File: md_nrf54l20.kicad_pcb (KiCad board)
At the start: 2 copper layers, 51.6 x 42 mm, 6 parts, among them J1 USB_C_Receptacle_USB2.0_16P, U1 nRF54L20

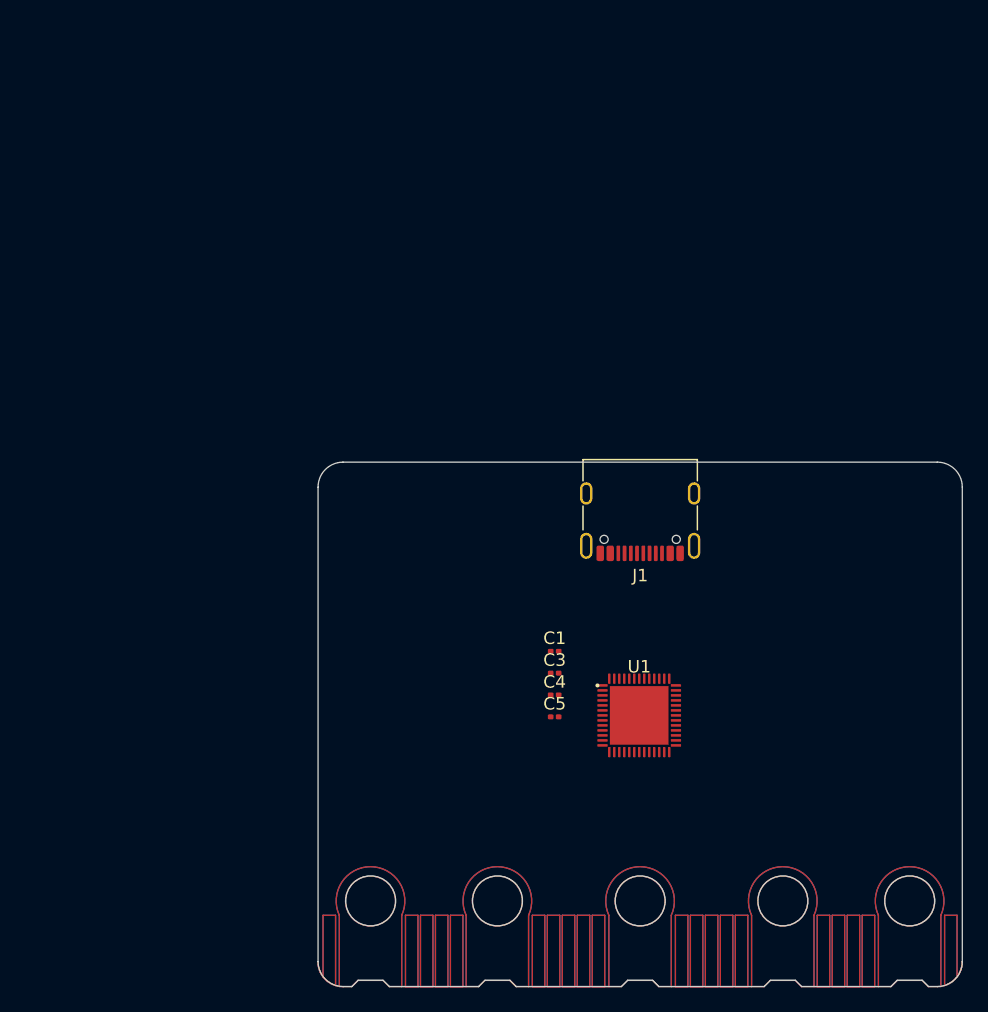
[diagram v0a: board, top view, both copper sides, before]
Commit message: Promote v2 and add Uno R3 shield headers
- circuit_v2.json -> circuit.json (single source); generated to the project
  root md_nrf54l20.kicad_sch; md_nrf54l20-v2.kicad_sch removed.
- Board: copied the ~/uno R3 form-factor PCB over md_nrf54l20.kicad_pcb
  (J1-J4 header sockets + 4 mounting holes); added Arduino_MountingHole.pretty
  and registered it in fp-lib-table.
- Wired the Uno headers to the nRF with function-correct pins: A0-A5 on ADC
  channels (AIN0-4 + AIN7), AREF on EXTREF, UART on D0/D1, SPI on D10-D13,
  PWM-capable pins on D3/D5/D6/D9/D10/D11; I2C SDA/SCL shared with A4/A5.
- Renumbered existing connectors so the Uno headers can be J1-J4: USB-C -> J5,
  SWD -> J6. Moved speaker PWM P1.06 -> P2.01 to free P1.06 for analog A4.

Co-Authored-By: Claude Opus 4.8 <noreply@anthropic.com>
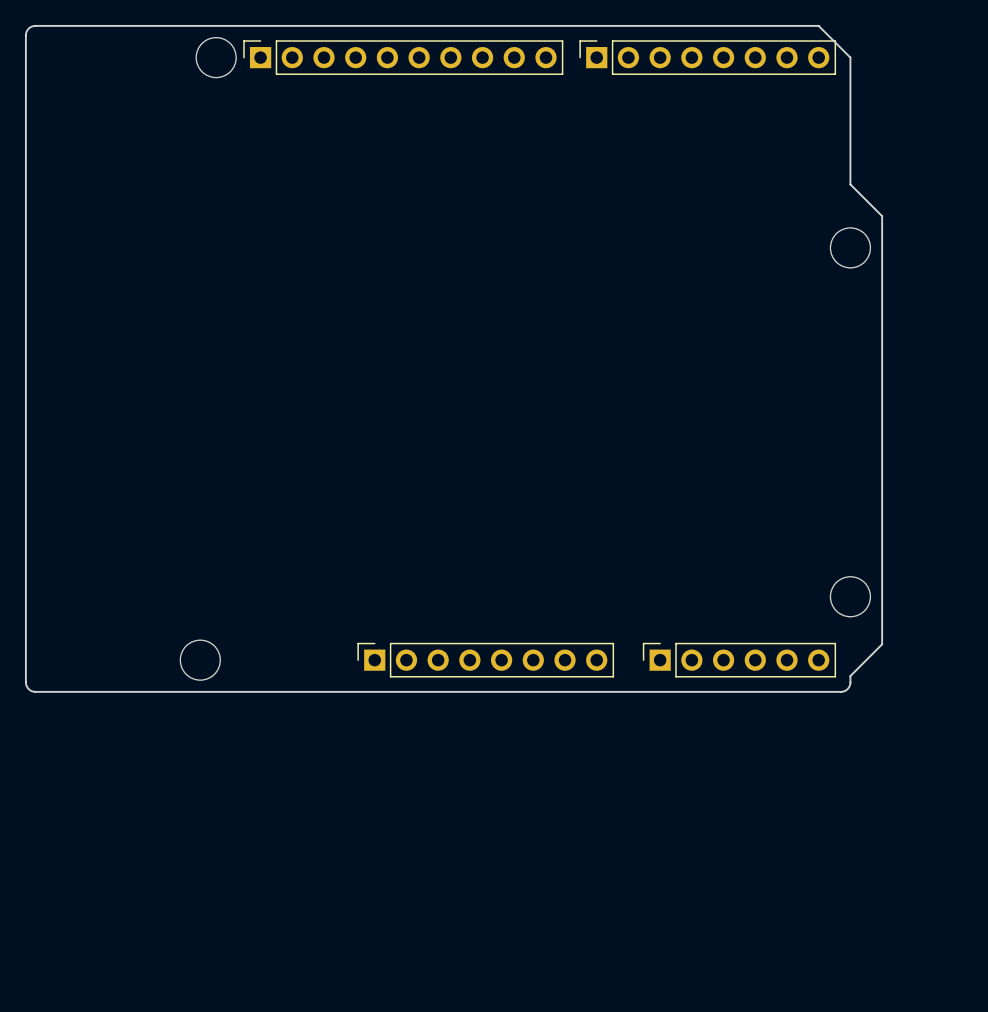
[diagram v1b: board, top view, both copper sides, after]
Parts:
- removed C1: 10uF, Capacitor_SMD:C_0201_0603Metric
- removed C3, C4, C5: 100nF, Capacitor_SMD:C_0201_0603Metric
- removed U1: nRF54L20, md_nrf54l20:QFN-52-1EP_6x6mm_P0.4mm_EP4.7x4.7mm
- added J2: Digital/PWM, Connector_PinSocket_2.54mm:PinSocket_1x10_P2.54mm_Vertical, F.Cu at (118.8, 49.2)
- added J3: Analog, Connector_PinSocket_2.54mm:PinSocket_1x06_P2.54mm_Vertical, F.Cu at (150.8, 97.5)
- added J4: Digital/PWM, Connector_PinSocket_2.54mm:PinSocket_1x08_P2.54mm_Vertical, F.Cu at (145.7, 49.2)
- added MH1: MountingHole_3.2mm, Arduino_MountingHole:MountingHole_3.2mm, F.Cu at (115.2, 49.2)
- added MH2: MountingHole_3.2mm, Arduino_MountingHole:MountingHole_3.2mm, F.Cu at (114.0, 97.5)
- added MH3: MountingHole_3.2mm, Arduino_MountingHole:MountingHole_3.2mm, F.Cu at (166.0, 64.4)
- added MH4: MountingHole_3.2mm, Arduino_MountingHole:MountingHole_3.2mm, F.Cu at (166.0, 92.4)
- J1: value USB_C_Receptacle_USB2.0_16P -> Power; footprint Connector_USB:USB_C_Receptacle_G-Switch_GT-USB-7010ASV -> Connector_PinSocket_2.54mm:PinSocket_1x08_P2.54mm_Vertical
- moved J1 24.6 mm to (127.9, 97.5), turned to 90 degrees
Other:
- board size 51.6 x 42 mm -> 68.6 x 53.3 mm
- board text added: "ICSP"
